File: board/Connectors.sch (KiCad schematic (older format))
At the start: 18 parts, among them J1 Conn_02x04_Counter_Clockwise, J2 Conn_02x05_Odd_Even, Q1 DMN65D8L-7, Q2 DMN65D8L-7, U2 FXL4TD245BQX

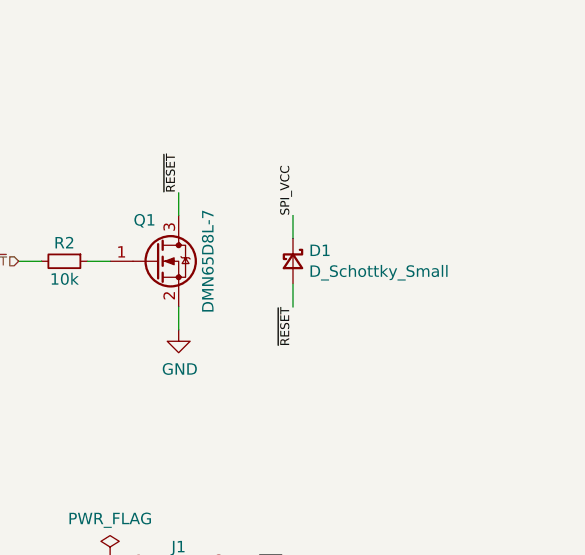
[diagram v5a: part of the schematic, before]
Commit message: Fixed the state of the BOM for the PCB being horrid
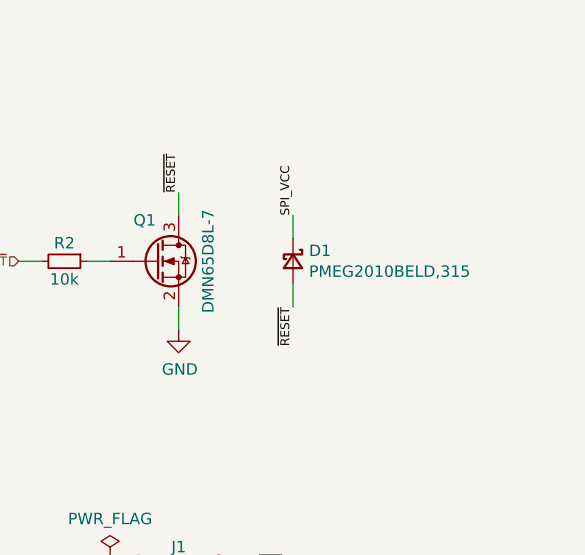
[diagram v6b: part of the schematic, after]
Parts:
- C1, C4, C5: MFR (none) -> Multicomp; MPN (none) -> MC0603B104J250CT; OC_FARNELL (none) -> 2310559; URL_FARNELL (none) -> https://uk.farnell.com/multicomp/mc0603b104j250ct/cap-0-1-f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
- D1: value D_Schottky_Small -> PMEG2010BELD,315; MFR (none) -> NXP; MPN (none) -> PMEG2010BELD,315; OC_FARNELL (none) -> 2191801; URL_FARNELL (none) -> https://uk.farnell.com/nexperia/pmeg2010beld-315/diode-rect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
- J1: MFR (none) -> Amphenol ICC; MPN (none) -> 75867-132LF; OC_FARNELL (none) -> 1924603; URL_FARNELL (none) -> https://uk.farnell.com/amphenol-icc/75867-132lf/connector-h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
- J2: MFR (none) -> Amphenol ICC; MPN (none) -> 20021321-00010C4LF; OC_FARNELL (none) -> 1865309; URL_FARNELL (none) -> https://uk.farnell.com/amphenol-icc-fci/20021321-00010c4lf/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
- JP1: MFR (none) -> Amphenol ICC; MPN (none) -> 10103593-0001LF; OC_FARNELL (none) -> 2293751; URL_FARNELL (none) -> https://uk.farnell.com/amphenol-icc-fci/10103593-0001lf/mic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
- Q1, Q2: MFR (none) -> Diodes Inc; MPN (none) -> DMN65D8L-7; OC_FARNELL (none) -> 2543546; URL_FARNELL (none) -> https://uk.farnell.com/diodes-inc/dmn65d8l-7/mosfet-n-ch-20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
- R1: MFR (none) -> Multicomp; MPN (none) -> MCWR06X1004FTL; OC_FARNELL (none) -> 2447285; URL_FARNELL (none) -> https://uk.farnell.com/multicomp/mcwr06x1004ftl/res-1m-1-0-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
- R13, R2: MFR (none) -> Multicomp; MPN (none) -> MC0063W0603110K; OC_FARNELL (none) -> 2130939; URL_FARNELL (none) -> https://uk.farnell.com/multicomp/mc0063w0603110k/res-10k-1-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
- U2: MFR (none) -> On Smi; MPN (none) -> FXL4TD245BQX; OC_FARNELL (none) -> 1495484; URL_FARNELL (none) -> https://uk.farnell.com/on-semiconductor/fxl4td245bqx/fxl-ti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
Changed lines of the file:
@@
 F 1 "USB-Micro-B" V 1400 6000 59  0000 C CNN
 F 2 "rhais_usb:MICRO-USB-B-(IN_PCB)" H 1650 6000 59  0001 C CNN
-F 3 "" H 1650 6000 59  0001 C CNN
+F 3 "https://cdn.amphenol-icc.com/media/wysiwyg/files/drawing/10103593.pdf" H 1650 6000 59  0001 C CNN
+F 4 "Amphenol ICC" H 1600 6000 50  0001 C CNN "MFR"
+F 5 "10103593-0001LF" H 1600 6000 50  0001 C CNN "MPN"
+F 6 "2293751" H 1600 6000 50  0001 C CNN "OC_FARNELL"
+F 7 "https://uk.farnell.com/amphenol-icc-fci/10103593-0001lf/micro-usb-2-0-type-b-receptacle/dp/2293751" H 1600 6000 50  0001 C CNN "URL_FARNELL"
 	1    1600 6000
 	1    0    0    -1
@@
 F 1 "0.1uF" H 2809 6045 50  0000 R CNN
 F 2 "rhais_rcl:C0603" H 2900 6000 50  0001 C CNN
-F 3 "~" H 2900 6000 50  0001 C CNN
+F 3 "http://www.farnell.com/datasheets/1870456.pdf" H 2900 6000 50  0001 C CNN
+F 4 "Multicomp" H 2900 6000 50  0001 C CNN "MFR"
+F 5 "MC0603B104J250CT" H 2900 6000 50  0001 C CNN "MPN"
+F 6 "2310559" H 2900 6000 50  0001 C CNN "OC_FARNELL"
+F 7 "https://uk.farnell.com/multicomp/mc0603b104j250ct/cap-0-1-f-25v-5-x7r-0603-reel/dp/2310559" H 2900 6000 50  0001 C CNN "URL_FARNELL"
 	1    2900 6000
 	1    0    0    1
@@
 F 1 "1M" H 3159 5955 50  0000 L CNN
 F 2 "rhais_rcl:R0603" H 3100 6000 50  0001 C CNN
-F 3 "~" H 3100 6000 50  0001 C CNN
+F 3 "http://www.farnell.com/datasheets/2860681.pdf" H 3100 6000 50  0001 C CNN
+F 4 "Multicomp" H 3100 6000 50  0001 C CNN "MFR"
+F 5 "MCWR06X1004FTL" H 3100 6000 50  0001 C CNN "MPN"
+F 6 "2447285" H 3100 6000 50  0001 C CNN "OC_FARNELL"
+F 7 "https://uk.farnell.com/multicomp/mcwr06x1004ftl/res-1m-1-0-1w-0603-thick-film/dp/2447285" H 3100 6000 50  0001 C CNN "URL_FARNELL"
 	1    3100 6000
 	1    0    0    -1
@@
 F 1 "Conn_02x04_Counter_Clockwise" H 9100 2650 50  0000 C CNN
 F 2 "DX-MON:75867-132LF" H 9450 2950 50  0001 C CNN
-F 3 "~" H 9450 2950 50  0001 C CNN
+F 3 "https://cdn.amphenol-icc.com/media/wysiwyg/files/drawing/75867.pdf" H 9450 2950 50  0001 C CNN
+F 4 "Amphenol ICC" H 9450 2950 50  0001 C CNN "MFR"
+F 5 "75867-132LF" H 9450 2950 50  0001 C CNN "MPN"
+F 6 "1924603" H 9450 2950 50  0001 C CNN "OC_FARNELL"
+F 7 "https://uk.farnell.com/amphenol-icc/75867-132lf/connector-header-8-position-2/dp/1924603" H 9450 2950 50  0001 C CNN "URL_FARNELL"
 	1    9450 2950
 	1    0    0    -1
@@
 F 1 "FXL4TD245BQX" H 7500 1950 50  0000 C CNN
 F 2 "rhais_package-qfn:DQFN16_1EP_2.5x3.5mm_P0.5mm" H 7500 2500 50  0001 C CNN
-F 3 "https://www.farnell.com/datasheets/2298347.pdf" H 7500 2500 50  0001 C CNN
+F 3 "https://www.onsemi.com/pub/Collateral/FXL4TD245-D.pdf" H 7500 2500 50  0001 C CNN
+F 4 "On Smi" H 7500 2500 50  0001 C CNN "MFR"
+F 5 "FXL4TD245BQX" H 7500 2500 50  0001 C CNN "MPN"
+F 6 "1495484" H 7500 2500 50  0001 C CNN "OC_FARNELL"
+F 7 "https://uk.farnell.com/on-semiconductor/fxl4td245bqx/fxl-tiny-translator-smd-dqfn-16/dp/1495484" H 7500 2500 50  0001 C CNN "URL_FARNELL"
 	1    7500 2500
 	1    0    0    -1
@@
 F 1 "0.1uF" H 6192 2455 50  0000 L CNN
 F 2 "rhais_rcl:C0603" H 6100 2500 50  0001 C CNN
-F 3 "~" H 6100 2500 50  0001 C CNN
+F 3 "http://www.farnell.com/datasheets/1870456.pdf" H 6100 2500 50  0001 C CNN
+F 4 "Multicomp" H 6100 2500 50  0001 C CNN "MFR"
+F 5 "MC0603B104J250CT" H 6100 2500 50  0001 C CNN "MPN"
+F 6 "2310559" H 6100 2500 50  0001 C CNN "OC_FARNELL"
+F 7 "https://uk.farnell.com/multicomp/mc0603b104j250ct/cap-0-1-f-25v-5-x7r-0603-reel/dp/2310559" H 6100 2500 50  0001 C CNN "URL_FARNELL"
 	1    6100 2500
 	1    0    0    -1
@@
 F 1 "0.1uF" H 5809 2545 50  0000 R CNN
 F 2 "rhais_rcl:C0603" H 5900 2500 50  0001 C CNN
-F 3 "~" H 5900 2500 50  0001 C CNN
+F 3 "http://www.farnell.com/datasheets/1870456.pdf" H 5900 2500 50  0001 C CNN
+F 4 "Multicomp" H 5900 2500 50  0001 C CNN "MFR"
+F 5 "MC0603B104J250CT" H 5900 2500 50  0001 C CNN "MPN"
+F 6 "2310559" H 5900 2500 50  0001 C CNN "OC_FARNELL"
+F 7 "https://uk.farnell.com/multicomp/mc0603b104j250ct/cap-0-1-f-25v-5-x7r-0603-reel/dp/2310559" H 5900 2500 50  0001 C CNN "URL_FARNELL"
 	1    5900 2500
 	1    0    0    1
@@
 F 1 "DMN65D8L-7" V 9600 1500 50  0000 C TNN
 F 2 "rhais_package-smd:SOT-23" H 9600 1600 50  0001 C CNN
-F 3 "https://www.farnell.com/datasheets/2040106.pdf" H 9400 1500 50  0001 C CNN
+F 3 "https://www.diodes.com/assets/Datasheets/DMN65D8L.pdf" H 9400 1500 50  0001 C CNN
+F 4 "Diodes Inc" H 9400 1500 50  0001 C CNN "MFR"
+F 5 "DMN65D8L-7" H 9400 1500 50  0001 C CNN "MPN"
+F 6 "2543546" H 9400 1500 50  0001 C CNN "OC_FARNELL"
+F 7 "https://uk.farnell.com/diodes-inc/dmn65d8l-7/mosfet-n-ch-20v-sot-23-3/dp/2543546" H 9400 1500 50  0001 C CNN "URL_FARNELL"
 	1    9400 1500
 	1    0    0    -1
@@
 F 1 "10k" V 9050 1500 50  0000 C TNN
 F 2 "rhais_rcl:R0603" H 9000 1500 50  0001 C CNN
-F 3 "~" H 9000 1500 50  0001 C CNN
+F 3 "http://www.farnell.com/datasheets/1788326.pdf" H 9000 1500 50  0001 C CNN
+F 4 "Multicomp" H 9000 1500 50  0001 C CNN "MFR"
+F 5 "MC0063W0603110K" H 9000 1500 50  0001 C CNN "MPN"
+F 6 "2130939" H 9000 1500 50  0001 C CNN "OC_FARNELL"
+F 7 "https://uk.farnell.com/multicomp/mc0063w0603110k/res-10k-1-0-063w-0603-thick-film/dp/2130939" H 9000 1500 50  0001 C CNN "URL_FARNELL"
 	1    9000 1500
 	0    1    1    0
@@
 P 10000 1500
 F 0 "D1" V 9954 1570 50  0000 L CNN
-F 1 "D_Schottky_Small" V 10045 1570 50  0000 L CNN
+F 1 "PMEG2010BELD,315" V 10045 1570 50  0000 L CNN
 F 2 "DX-MON:SOD882D_DFN1006D-2" V 10000 1500 50  0001 C CNN
-F 3 "https://www.farnell.com/datasheets/1996746.pdf" V 10000 1500 50  0001 C CNN
+F 3 "https://assets.nexperia.com/documents/data-sheet/PMEG2010BELD.pdf" V 10000 1500 50  0001 C CNN
+F 4 "NXP" H 10000 1500 50  0001 C CNN "MFR"
+F 5 "PMEG2010BELD,315" H 10000 1500 50  0001 C CNN "MPN"
+F 6 "2191801" H 10000 1500 50  0001 C CNN "OC_FARNELL"
+F 7 "https://uk.farnell.com/nexperia/pmeg2010beld-315/diode-rectifier-20v-1a-sod882d/dp/2191801" H 10000 1500 50  0001 C CNN "URL_FARNELL"
 	1    10000 1500
 	0    1    1    0
@@
 F 1 "Conn_02x05_Odd_Even" H 2600 2826 50  0000 C CNN
 F 2 "rhais_connector-pinheader:PinSocket_2x05_P1.27mm_Vertical_SMD" H 2550 2500 50  0001 C CNN
-F 3 "~" H 2550 2500 50  0001 C CNN
+F 3 "https://cdn.amphenol-icc.com/media/wysiwyg/files/drawing/20021321.pdf" H 2550 2500 50  0001 C CNN
+F 4 "Amphenol ICC" H 2550 2500 50  0001 C CNN "MFR"
+F 5 "20021321-00010C4LF" H 2550 2500 50  0001 C CNN "MPN"
+F 6 "1865309" H 2550 2500 50  0001 C CNN "OC_FARNELL"
+F 7 "https://uk.farnell.com/amphenol-icc-fci/20021321-00010c4lf/receptacle-vert-1-27mm-smt-10way/dp/1865309" H 2550 2500 50  0001 C CNN "URL_FARNELL"
 	1    2550 2500
 	-1   0    0    -1
@@
 F 1 "DMN65D8L-7" V 6300 6000 50  0000 C TNN
 F 2 "rhais_package-smd:SOT-23" H 6300 6100 50  0001 C CNN
-F 3 "https://www.farnell.com/datasheets/2040106.pdf" H 6100 6000 50  0001 C CNN
+F 3 "https://www.diodes.com/assets/Datasheets/DMN65D8L.pdf" H 6100 6000 50  0001 C CNN
+F 4 "Diodes Inc" H 6100 6000 50  0001 C CNN "MFR"
+F 5 "DMN65D8L-7" H 6100 6000 50  0001 C CNN "MPN"
+F 6 "2543546" H 6100 6000 50  0001 C CNN "OC_FARNELL"
+F 7 "https://uk.farnell.com/diodes-inc/dmn65d8l-7/mosfet-n-ch-20v-sot-23-3/dp/2543546" H 6100 6000 50  0001 C CNN "URL_FARNELL"
 	1    6100 6000
 	-1   0    0    -1
@@
 F 1 "10k" V 6395 6000 50  0000 C CNN
 F 2 "rhais_rcl:R0603" H 6500 6000 50  0001 C CNN
-F 3 "~" H 6500 6000 50  0001 C CNN
+F 3 "http://www.farnell.com/datasheets/1788326.pdf" H 6500 6000 50  0001 C CNN
+F 4 "Multicomp" H 6500 6000 50  0001 C CNN "MFR"
+F 5 "MC0063W0603110K" H 6500 6000 50  0001 C CNN "MPN"
+F 6 "2130939" H 6500 6000 50  0001 C CNN "OC_FARNELL"
+F 7 "https://uk.farnell.com/multicomp/mc0063w0603110k/res-10k-1-0-063w-0603-thick-film/dp/2130939" H 6500 6000 50  0001 C CNN "URL_FARNELL"
 	1    6500 6000
 	0    1    1    0
@@
 F 2 "Symbol:WEEE-Logo_4.2x6mm_SilkScreen" H 8500 4960 50  0001 C CNN
 F 3 "~" H 8500 4960 50  0001 C CNN
+F 4 "" H 8500 4950 50  0001 C CNN "MFR"
+F 5 "" H 8500 4950 50  0001 C CNN "MPN"
+F 6 "" H 8500 4950 50  0001 C CNN "OC_FARNELL"
+F 7 "" H 8500 4950 50  0001 C CNN "URL_FARNELL"
 	1    8500 4950
 	1    0    0    -1

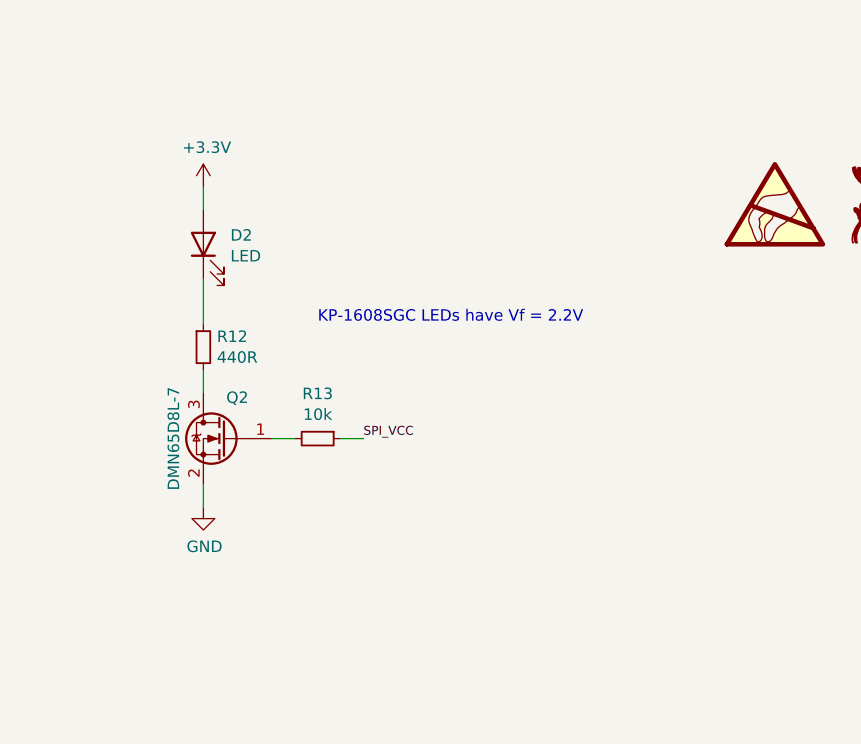
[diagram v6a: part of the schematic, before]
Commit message: Added a SPI present signal for the external bus to the CPU to make detection easier
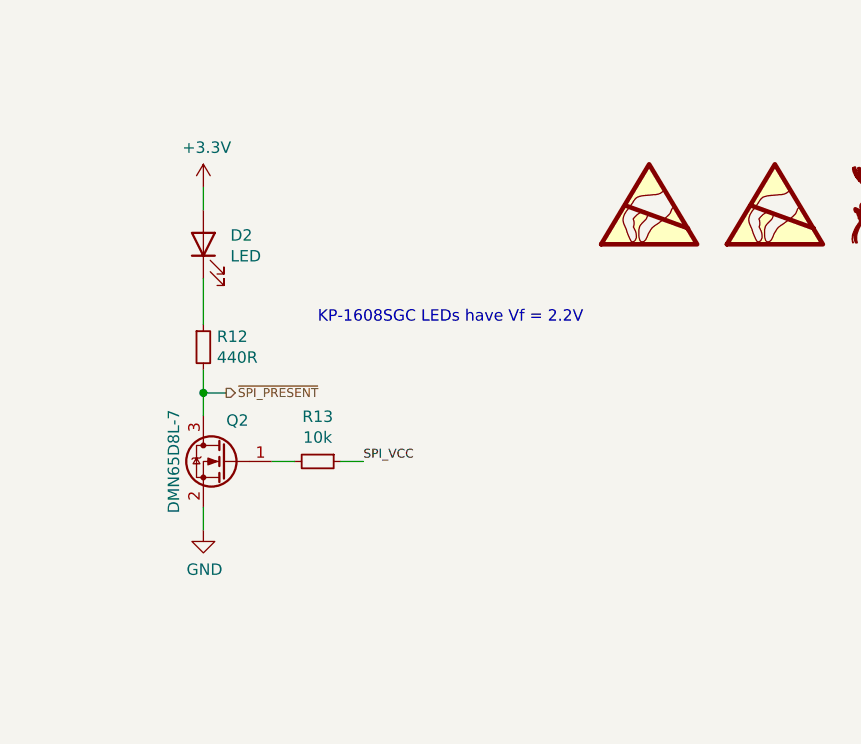
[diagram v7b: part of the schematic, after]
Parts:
- added SYM2: SYM_ESD_Small, Symbol:ESD-Logo_6.6x6mm_SilkScreen, symbol Graphic:SYM_ESD_Large
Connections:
- net ~SPI_PRESENT: now reaches Q2.3 (D), R12.2
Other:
- moved on the sheet: Q2, R13
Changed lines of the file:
@@
 L power:GND #PWR?
 U 1 1 5F95431F
-P 6000 6300
+P 6000 6400
 AR Path="/5F6E308F/5F95431F" Ref="#PWR?"  Part="1"
 AR Path="/5F0A82B6/5F95431F" Ref="#PWR039"  Part="1"
-F 0 "#PWR039" H 6000 6050 50  0001 C CNN
-F 1 "GND" H 6005 6127 50  0000 C CNN
-F 2 "" H 6000 6300 50  0001 C CNN
-F 3 "" H 6000 6300 50  0001 C CNN
-	1    6000 6300
+F 0 "#PWR039" H 6000 6150 50  0001 C CNN
+F 1 "GND" H 6005 6227 50  0000 C CNN
+F 2 "" H 6000 6400 50  0001 C CNN
+F 3 "" H 6000 6400 50  0001 C CNN
+	1    6000 6400
 	1    0    0    -1
 $EndComp
 Wire Wire Line
 	6000 5700 6000 5800
-Text Label 6700 6000 0    39   ~ 0
+Text Label 6700 6100 0    39   ~ 0
 SPI_VCC
 $Comp
 L Device:Q_NMOS_GSD Q2
 U 1 1 5F958118
-P 6100 6000
-F 0 "Q2" H 6100 6150 50  0000 R BNN
-F 1 "DMN65D8L-7" V 6300 6000 50  0000 C TNN
-F 2 "rhais_package-smd:SOT-23" H 6300 6100 50  0001 C CNN
-F 3 "https://www.diodes.com/assets/Datasheets/DMN65D8L.pdf" H 6100 6000 50  0001 C CNN
-F 4 "Diodes Inc" H 6100 6000 50  0001 C CNN "MFR"
-F 5 "DMN65D8L-7" H 6100 6000 50  0001 C CNN "MPN"
-F 6 "2543546" H 6100 6000 50  0001 C CNN "OC_FARNELL"
-F 7 "https://uk.farnell.com/diodes-inc/dmn65d8l-7/mosfet-n-ch-20v-sot-23-3/dp/2543546" H 6100 6000 50  0001 C CNN "URL_FARNELL"
-	1    6100 6000
+P 6100 6100
+F 0 "Q2" H 6100 6250 50  0000 R BNN
+F 1 "DMN65D8L-7" V 6300 6100 50  0000 C TNN
+F 2 "rhais_package-smd:SOT-23" H 6300 6200 50  0001 C CNN
+F 3 "https://www.diodes.com/assets/Datasheets/DMN65D8L.pdf" H 6100 6100 50  0001 C CNN
+F 4 "Diodes Inc" H 6100 6100 50  0001 C CNN "MFR"
+F 5 "DMN65D8L-7" H 6100 6100 50  0001 C CNN "MPN"
+F 6 "2543546" H 6100 6100 50  0001 C CNN "OC_FARNELL"
+F 7 "https://uk.farnell.com/diodes-inc/dmn65d8l-7/mosfet-n-ch-20v-sot-23-3/dp/2543546" H 6100 6100 50  0001 C CNN "URL_FARNELL"
+	1    6100 6100
 	-1   0    0    -1
 $EndComp
 Wire Wire Line
-	6000 6300 6000 6200
+	6000 6400 6000 6300
 $Comp
 L Device:R_Small R?
 U 1 1 5F964FD0
-P 6500 6000
+P 6500 6100
 AR Path="/5F6E308F/5F964FD0" Ref="R?"  Part="1"
 AR Path="/5F0A82B6/5F964FD0" Ref="R13"  Part="1"
-F 0 "R13" V 6304 6000 50  0000 C CNN
-F 1 "10k" V 6395 6000 50  0000 C CNN
-F 2 "rhais_rcl:R0603" H 6500 6000 50  0001 C CNN
-F 3 "http://www.farnell.com/datasheets/1788326.pdf" H 6500 6000 50  0001 C CNN
-F 4 "Multicomp" H 6500 6000 50  0001 C CNN "MFR"
-F 5 "MC0063W0603110K" H 6500 6000 50  0001 C CNN "MPN"
-F 6 "2130939" H 6500 6000 50  0001 C CNN "OC_FARNELL"
-F 7 "https://uk.farnell.com/multicomp/mc0063w0603110k/res-10k-1-0-063w-0603-thick-film/dp/2130939" H 6500 6000 50  0001 C CNN "URL_FARNELL"
-	1    6500 6000
+F 0 "R13" V 6304 6100 50  0000 C CNN
+F 1 "10k" V 6395 6100 50  0000 C CNN
+F 2 "rhais_rcl:R0603" H 6500 6100 50  0001 C CNN
+F 3 "http://www.farnell.com/datasheets/1788326.pdf" H 6500 6100 50  0001 C CNN
+F 4 "Multicomp" H 6500 6100 50  0001 C CNN "MFR"
+F 5 "MC0063W0603110K" H 6500 6100 50  0001 C CNN "MPN"
+F 6 "2130939" H 6500 6100 50  0001 C CNN "OC_FARNELL"
+F 7 "https://uk.farnell.com/multicomp/mc0063w0603110k/res-10k-1-0-063w-0603-thick-film/dp/2130939" H 6500 6100 50  0001 C CNN "URL_FARNELL"
+	1    6500 6100
 	0    1    1    0
 $EndComp
 Wire Wire Line
-	6300 6000 6400 6000
+	6300 6100 6400 6100
 Wire Wire Line
-	6700 6000 6600 6000
+	6700 6100 6600 6100
 Text Notes 6500 5500 0    50   ~ 0
 KP-1608SGC LEDs have Vf = 2.2V
@@
 Wire Wire Line
 	1500 6500 1500 6600
+$Comp
+L Graphic:SYM_ESD_Large SYM2
+U 1 1 5FBF2016
+P 7950 4950
+F 0 "SYM2" H 7950 5090 50  0001 C CNN
+F 1 "SYM_ESD_Small" H 7950 4825 50  0001 C CNN
+F 2 "Symbol:ESD-Logo_6.6x6mm_SilkScreen" H 7950 4960 50  0001 C CNN
+F 3 "~" H 7950 4960 50  0001 C CNN
+F 4 "" H 7950 4950 50  0001 C CNN "MFR"
+F 5 "" H 7950 4950 50  0001 C CNN "MPN"
+F 6 "" H 7950 4950 50  0001 C CNN "OC_FARNELL"
+F 7 "" H 7950 4950 50  0001 C CNN "URL_FARNELL"
+	1    7950 4950
+	1    0    0    -1
+$EndComp
+Wire Wire Line
+	6000 5800 6100 5800
+Connection ~ 6000 5800
+Wire Wire Line
+	6000 5800 6000 5900
+Text HLabel 6100 5800 2    39   Output ~ 0
+~SPI_PRESENT
 $EndSCHEMATC
